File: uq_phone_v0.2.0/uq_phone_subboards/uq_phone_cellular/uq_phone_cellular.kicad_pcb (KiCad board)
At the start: 4 copper layers, 45 x 30.2 mm, 32 parts, among them J1 513382474, J2 513382474, J3 20279-001E-03, J4 20279-001E-03, U1 WP SNAP-IN BASE_6000636

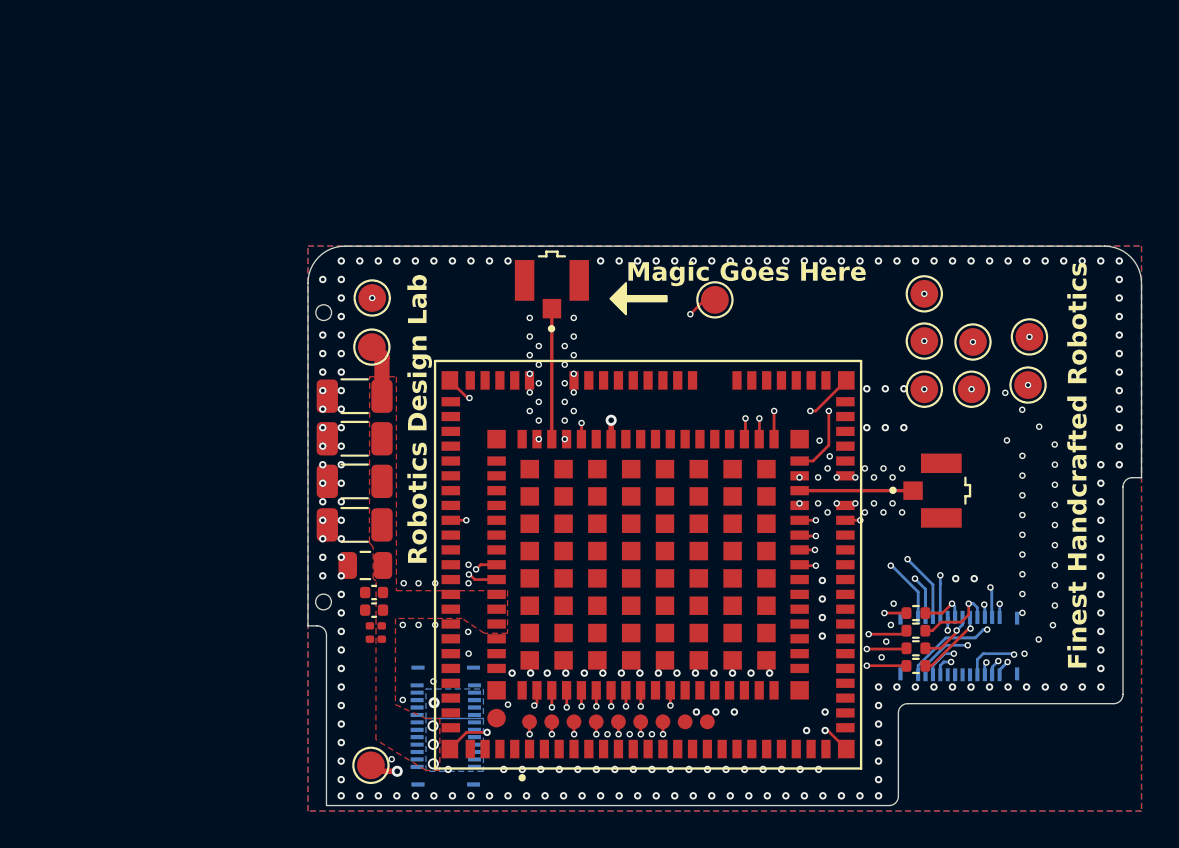
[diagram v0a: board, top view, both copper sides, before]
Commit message: New logic level shifters
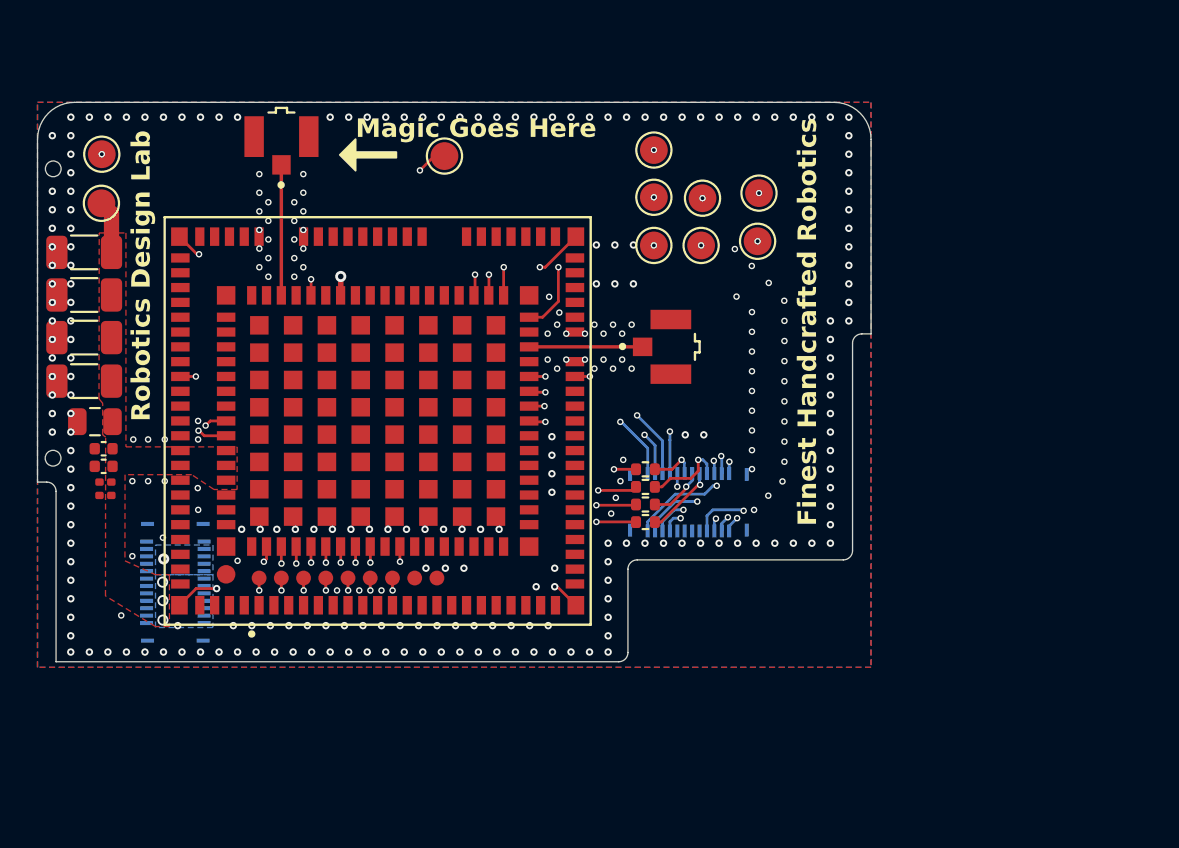
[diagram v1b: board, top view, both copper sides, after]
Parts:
- removed the TP4 at (86.6, 88.7)
- moved ? 16.5 mm to (69.4, 72.1)
- moved J3 16.5 mm to (81.8, 54.7)
- moved TP1 16.5 mm to (72.1, 55.7)
- moved TP8 16.5 mm to (107.5, 60.4)
- moved TP9 16.5 mm to (104.4, 60.6)
- moved TP2 16.5 mm to (72.0, 58.3)
- moved TP3 16.5 mm to (90.6, 55.8)
- moved TP7 16.5 mm to (107.5, 57.8)
- moved C1 16.5 mm to (72.2, 72.5)
- moved C3 16.5 mm to (72.3, 74.1)
- moved C4 16.5 mm to (72.3, 73.4)
- moved C5 16.5 mm to (71.7, 70.1)
- moved C7 16.5 mm to (71.1, 67.9)
- moved C9 16.5 mm to (71.1, 61.0)
- moved J1 16.5 mm to (103.7, 74.5)
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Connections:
- J1 pad 13: MOB_DCD -> MOB_DTR
- J1 pad 14: MOB_DTR -> MOB_DCD
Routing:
- net +1.8V: track 26.7 -> 20.2 mm, vias 3 -> 2
- net GND: vias 300 -> 296

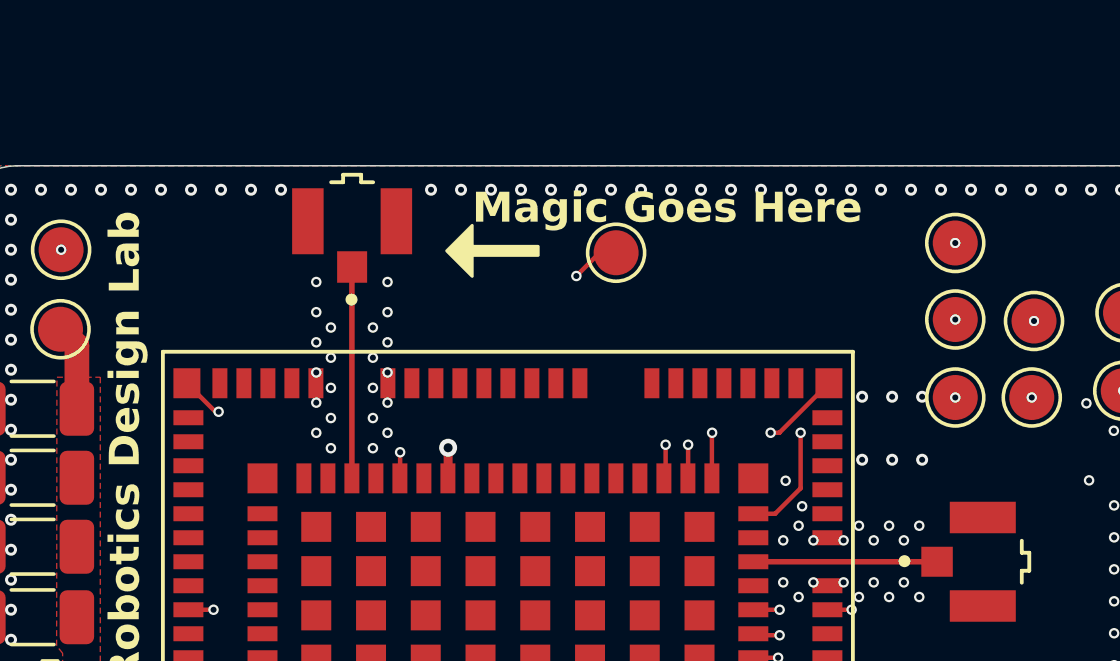
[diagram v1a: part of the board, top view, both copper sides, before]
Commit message: Add GNSS antenna for sag
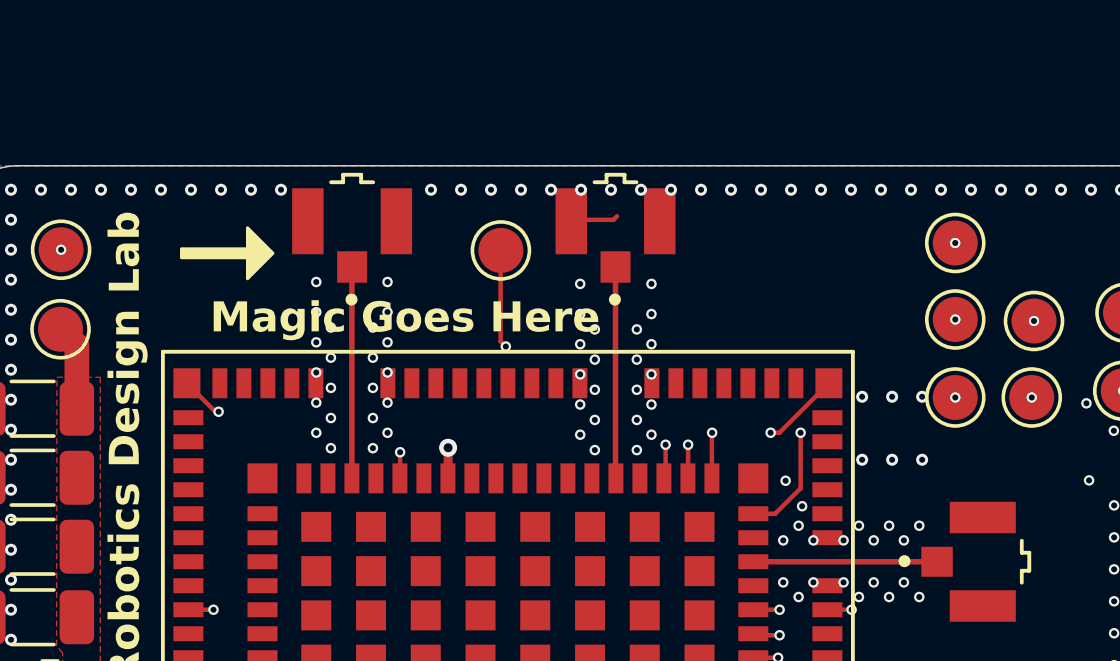
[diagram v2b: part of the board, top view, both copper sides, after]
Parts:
- added J5: 20279-001E-03, 20279-001E-03:IPEX_20279-001E-03, F.Cu at (90.5, 54.7)
- moved TP3 3.84 mm to (86.7, 55.7)
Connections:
- U1 pad 38: unconnected-(U1A-RF_GNSS-Pad38) -> MOB_GNSS_ANT
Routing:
- net MOB_GNSS_ANT: track 0.00 -> 7.05 mm
- net Net-(U1A-TP1_BOOTPIN): track 10.8 -> 9.30 mm
- net (no net): track 0.00 -> 1.42 mm
- net GND: vias 296 -> 318

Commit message: Routing improvements
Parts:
- moved R3 0.75 mm to (101.9, 72.2)
- moved R1 0.75 mm to (101.9, 73.1)
- moved R4 0.74 mm to (102.0, 74.1)
- moved R2 0.73 mm to (101.9, 75.0)
- moved C3 0.46 mm to (71.8, 74.1)
- moved C4 0.46 mm to (71.8, 73.4)
- moved C1 0.26 mm to (71.9, 72.6)
- moved C2 0.26 mm to (71.9, 71.6)
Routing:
- net Net-(U1A-UART1_RX): track 29.4 -> 22.5 mm
- net GND: track 8.01 -> 1.45 mm, vias 318 -> 359
- net Net-(U1A-UART1_TX): track 29.0 -> 23.4 mm
- net Net-(U1A-UART1_CTS): track 28.7 -> 24.3 mm
- net Net-(U1A-UART1_RTS): track 28.4 -> 24.6 mm
- net MOB_RI: track 32.0 -> 29.2 mm
- net MOB_AUD_IN: track 33.6 -> 31.7 mm
- net MOB_PWR: track 43.5 -> 41.6 mm
- net MOB_AUD_OUT: track 32.4 -> 30.6 mm
- net MOB_SAFE_PWR_REMOVE_L: track 43.8 -> 42.1 mm
- net MOB_RST: track 24.9 -> 23.2 mm
- net (no net): track 1.42 -> 0.00 mm
- net Net-(U1A-J3): track 36.7 -> 35.5 mm
- net Net-(U1A-J5): track 38.0 -> 36.8 mm
- net Net-(U1A-J4): track 39.1 -> 38.0 mm
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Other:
- board text added: "More Magic"

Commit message: Cleaning up adn fixing massive mistake
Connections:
- J1 pad 5: unconnected-(J1-Pad5) -> GND
- J1 pad 6: unconnected-(J1-Pad6) -> GND
- J1 pad 7: unconnected-(J1-Pad7) -> GND
- J1 pad 8: unconnected-(J1-Pad8) -> GND
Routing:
- net GND: track 1.45 -> 37.2 mm, vias 359 -> 350
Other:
- board text added: "J.Wood P.Pounds"
- board text added: "UQ RDL"
